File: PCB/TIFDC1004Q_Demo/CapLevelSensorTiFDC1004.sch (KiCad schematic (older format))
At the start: 11 parts, among them J1 Conn_01x02_Female, J2 Conn_01x02_Female, J3 Conn_01x02_Female, J4 Conn_01x02_Female, J5 Conn_01x04_Male, U1 FDC1004

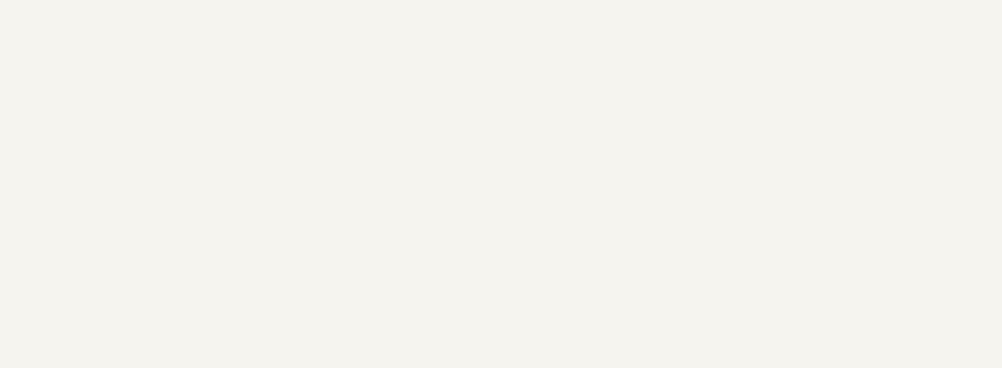
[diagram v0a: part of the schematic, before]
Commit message: updating BOM info
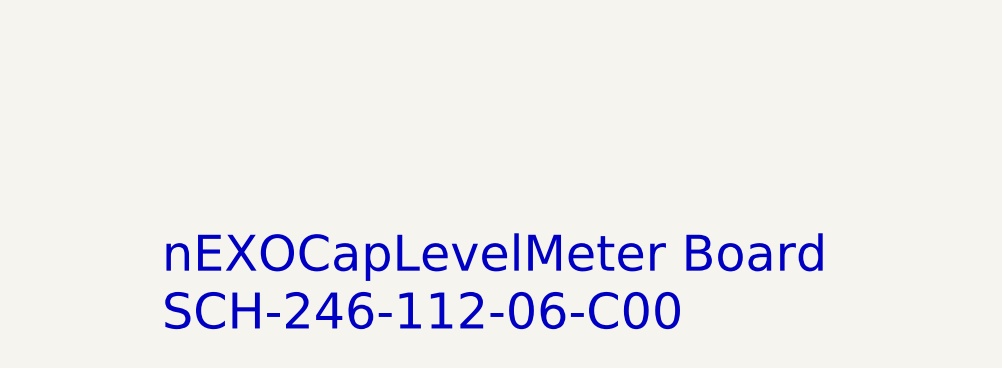
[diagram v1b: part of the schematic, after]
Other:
- note added: "nEXOCapLevelMeter Board\nSCH-246-112-06-C00"
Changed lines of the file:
@@
 F 1 "FDC1004" H 5850 3024 50  0000 C CNN
 F 2 "Package_SO:VSSOP-10_3x3mm_P0.5mm" H 5600 2700 50  0001 C CNN
-F 3 "" H 5600 2700 50  0001 C CNN
+F 3 "https://www.digikey.com/en/products/detail/FDC1004QDGSRQ1/296-42334-1-ND/5356920?itemSeq=374797743" H 5600 2700 50  0001 C CNN
 	1    5850 2750
 	1    0    0    -1
@@
 F 1 "Conn_01x02_Female" H 4142 2244 50  0000 C CNN
 F 2 "TerminalBlock_Phoenix:TerminalBlock_Phoenix_PT-1,5-2-3.5-H_1x02_P3.50mm_Horizontal" H 4250 2150 50  0001 C CNN
-F 3 "~" H 4250 2150 50  0001 C CNN
+F 3 "https://www.digikey.com/en/products/detail/YO0201500000G/609-4725-ND/4242160?itemSeq=374797741" H 4250 2150 50  0001 C CNN
 	1    4250 2150
 	-1   0    0    -1
@@
 F 1 "Conn_01x02_Female" H 4142 2644 50  0000 C CNN
 F 2 "TerminalBlock_Phoenix:TerminalBlock_Phoenix_PT-1,5-2-3.5-H_1x02_P3.50mm_Horizontal" H 4250 2550 50  0001 C CNN
-F 3 "~" H 4250 2550 50  0001 C CNN
+F 3 "https://www.digikey.com/en/products/detail/YO0201500000G/609-4725-ND/4242160?itemSeq=374797741" H 4250 2550 50  0001 C CNN
 	1    4250 2550
 	-1   0    0    -1
@@
 F 1 "Conn_01x02_Female" H 4142 3044 50  0000 C CNN
 F 2 "TerminalBlock_Phoenix:TerminalBlock_Phoenix_PT-1,5-2-3.5-H_1x02_P3.50mm_Horizontal" H 4250 2950 50  0001 C CNN
-F 3 "~" H 4250 2950 50  0001 C CNN
+F 3 "https://www.digikey.com/en/products/detail/YO0201500000G/609-4725-ND/4242160?itemSeq=374797741" H 4250 2950 50  0001 C CNN
 	1    4250 2950
 	-1   0    0    -1
@@
 F 1 "Conn_01x02_Female" H 4142 3444 50  0000 C CNN
 F 2 "TerminalBlock_Phoenix:TerminalBlock_Phoenix_PT-1,5-2-3.5-H_1x02_P3.50mm_Horizontal" H 4250 3350 50  0001 C CNN
-F 3 "~" H 4250 3350 50  0001 C CNN
+F 3 "https://www.digikey.com/en/products/detail/YO0201500000G/609-4725-ND/4242160?itemSeq=374797741" H 4250 3350 50  0001 C CNN
 	1    4250 3350
 	-1   0    0    -1
@@
 F 1 "0.1uF" H 6400 2650 50  0000 L CNN
 F 2 "Capacitor_SMD:C_0805_2012Metric_Pad1.18x1.45mm_HandSolder" H 6550 2950 50  0001 C CNN
-F 3 "~" H 6550 2950 50  0001 C CNN
+F 3 "https://www.digikey.com/en/products/detail/08055C104KAT4A/478-10836-1-ND/7536355?itemSeq=374797745" H 6550 2950 50  0001 C CNN
 F 4 "X7R" H 6550 2950 50  0001 C CNN "Type"
 	1    6550 2950
@@
 F 1 "1uF" H 6700 2650 50  0000 L CNN
 F 2 "Capacitor_SMD:C_0805_2012Metric_Pad1.18x1.45mm_HandSolder" H 6750 2950 50  0001 C CNN
-F 3 "~" H 6750 2950 50  0001 C CNN
+F 3 "https://www.digikey.com/en/products/detail/885012207051/732-7664-1-ND/5454291?itemSeq=374797744" H 6750 2950 50  0001 C CNN
 F 4 "X7R" H 6750 2950 50  0001 C CNN "Type"
 	1    6750 2950
@@
 F 1 "10K" H 6750 3050 50  0000 L CNN
 F 2 "Resistor_SMD:R_0805_2012Metric_Pad1.20x1.40mm_HandSolder" H 6850 2750 50  0001 C CNN
-F 3 "~" H 6850 2750 50  0001 C CNN
+F 3 "https://www.digikey.com/en/products/detail/RNCP0805FTD10K0/RNCP0805FTD10K0CT-ND/2240601?itemSeq=374797742" H 6850 2750 50  0001 C CNN
 	1    6850 2750
 	1    0    0    -1
@@
 F 1 "10K" H 6950 3050 50  0000 L CNN
 F 2 "Resistor_SMD:R_0805_2012Metric_Pad1.20x1.40mm_HandSolder" H 7000 2750 50  0001 C CNN
-F 3 "~" H 7000 2750 50  0001 C CNN
+F 3 "https://www.digikey.com/en/products/detail/RNCP0805FTD10K0/RNCP0805FTD10K0CT-ND/2240601?itemSeq=374797742" H 7000 2750 50  0001 C CNN
 	1    7000 2750
 	1    0    0    -1
@@
 Wire Wire Line
 	6250 3350 6250 3050
+Text Notes 7000 7050 0    157  ~ 0
+nEXOCapLevelMeter Board\nSCH-246-112-06-C00
 $EndSCHEMATC
